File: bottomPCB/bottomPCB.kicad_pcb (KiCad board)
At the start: 2 copper layers, 184.8 x 132.4 mm, 48 parts, among them CN2 XT30UPB-F, J2 Conn_02x03_Odd_Even, J3 Conn_01x02, J4 Conn_02x03_Odd_Even, U1 ESP32-WROOM-32, U3 XT30_horizontal, U8 LM1117IMPX-3_3_NOPB, U9 LM1117IMPX-3_3_NOPB

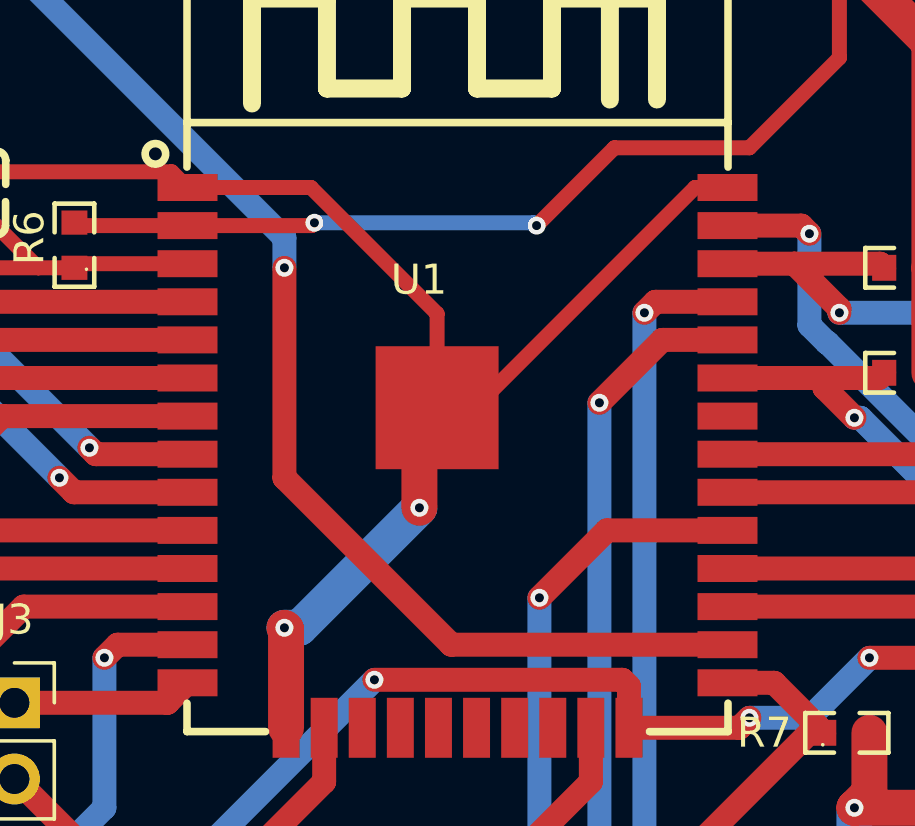
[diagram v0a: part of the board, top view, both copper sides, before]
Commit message: removed useless gnd traces
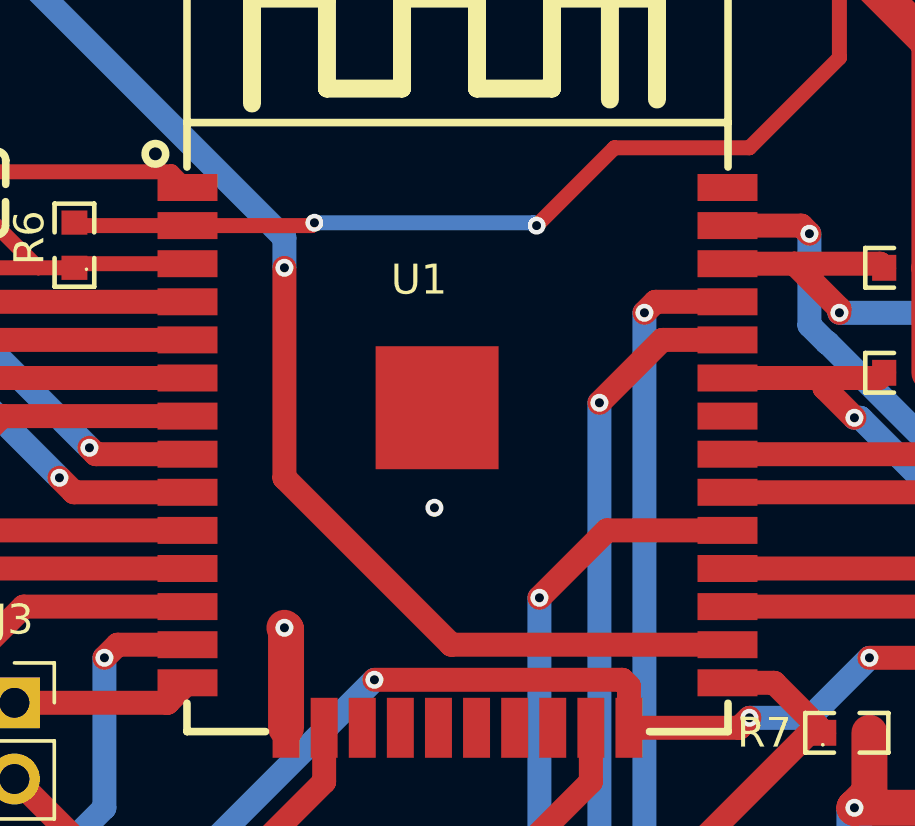
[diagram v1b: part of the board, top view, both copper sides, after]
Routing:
- net GND: track 109.5 -> 76.0 mm
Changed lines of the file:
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@@
-	)
-	(segment
-		(start 1.769622 7.823381)
-		(end 5.884042 7.823381)
-		(width 0.5)
-		(layer "F.Cu")
-		(net 1)
 	)
 	(segment
 		(start -14.539999 27.579999)
 		(end -14.5 27.54)
-		(width 1.2)
-		(layer "F.Cu")
-		(net 1)
-	)
-	(segment
-		(start 9.5 18.5)
-		(end 9.5 15.753404)
 		(width 1.2)
 		(layer "F.Cu")
@@
 	)
 	(segment
-		(start 18.689625 7.823381)
-		(end 19.769622 7.823381)
-		(width 0.5)
-		(layer "F.Cu")
-		(net 1)
-	)
-	(segment
 		(start -11.96 27.54)
 		(end -9.42 27.54)
@@
 	)
 	(segment
-		(start 5.884042 7.823381)
-		(end 10.089662 12.029001)
-		(width 0.5)
-		(layer "F.Cu")
-		(net 1)
-	)
-	(segment
 		(start 34.5 47.5)
 		(end 33.459995 46.459995)
@@
 	)
 	(segment
-		(start 11.349264 15.163742)
-		(end 18.689625 7.823381)
-		(width 0.5)
-		(layer "F.Cu")
-		(net 1)
-	)
-	(segment
 		(start 1.246217 7.299976)
 		(end 1.769622 7.823381)
@@
 		(start -5 7.299976)
 		(end 1.246217 7.299976)
-		(width 0.5)
-		(layer "F.Cu")
-		(net 1)
-	)
-	(segment
-		(start 10.089662 12.029001)
-		(end 10.089662 15.163742)
 		(width 0.5)
 		(layer "F.Cu")
@@
 	)
 	(via
-		(at 9.5 18.5)
+		(at 10 18.5)
 		(size 0.6)
 		(drill 0.3)
@@
 		(net 1)
 	)
-	(segment
-		(start 5 22.5)
-		(end 5.5 22.5)
-		(width 1.2)
-		(layer "B.Cu")
-		(net 1)
-	)
-	(segment
-		(start 5.5 22.5)
-		(end 9.5 18.5)
-		(width 1.2)
-		(layer "B.Cu")
-		(net 1)
-	)

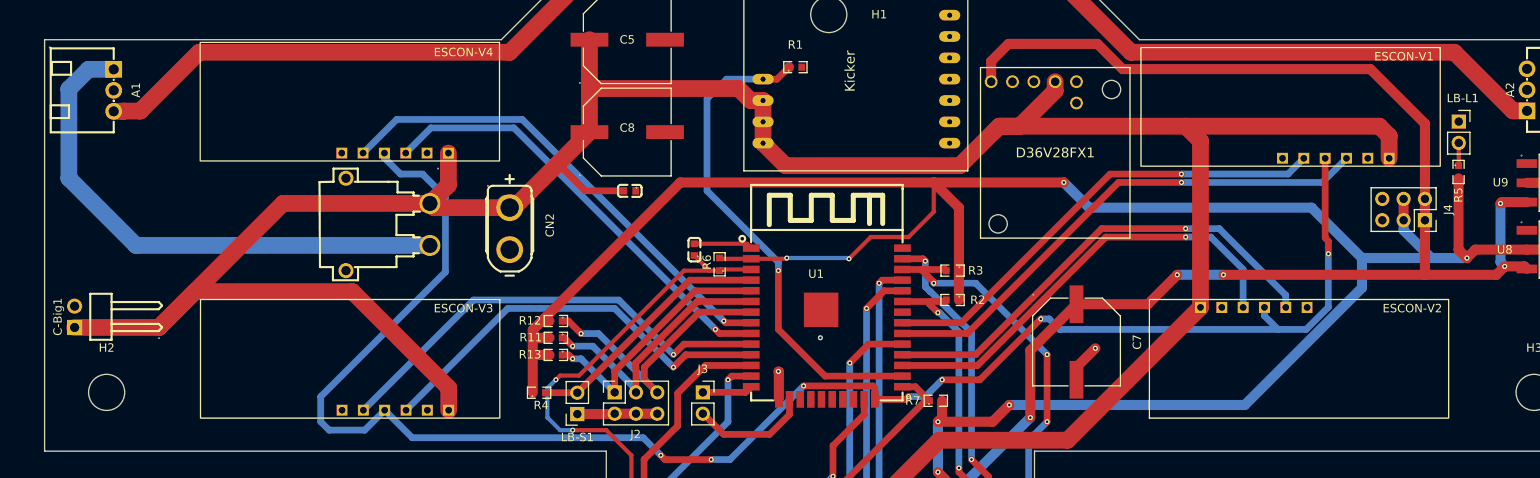
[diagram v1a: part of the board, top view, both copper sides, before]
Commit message: added silk screen (polarity, pinout)
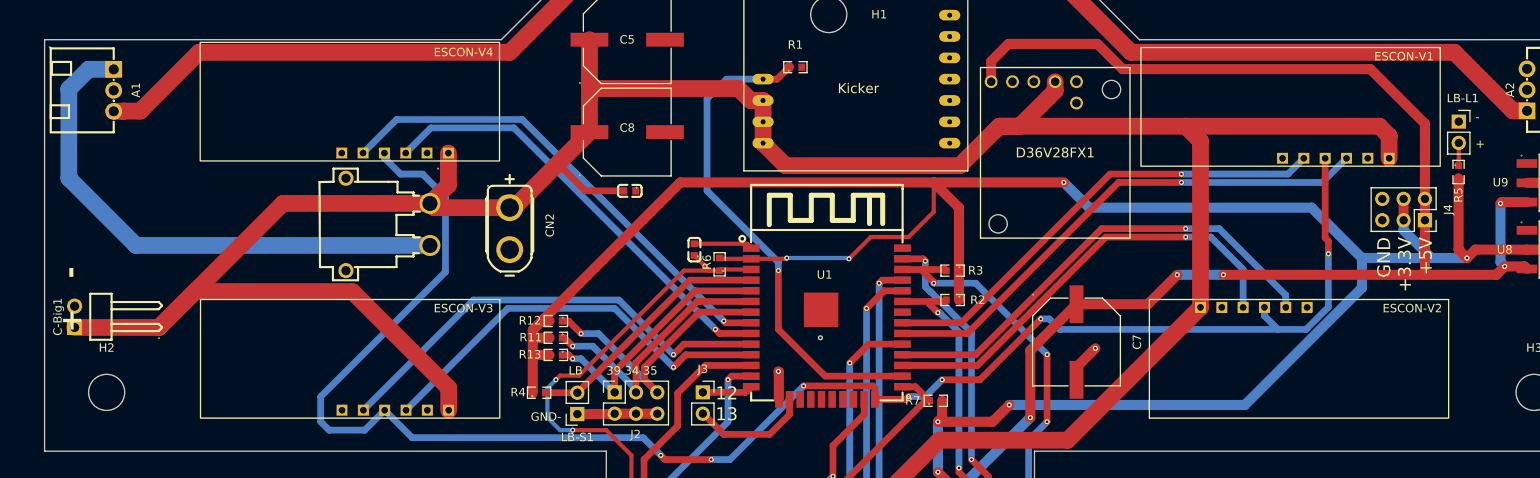
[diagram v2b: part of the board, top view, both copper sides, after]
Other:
- board text added: "- +"
- board text added: "12 13"
- board text added: "39 34 35"
- board text added: "GND +3.3V +5V"
- board text added: "GND-"
- board text added: "LB"
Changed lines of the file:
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@@
 		(tags "WIFIM-SMD_ESP32-WROOM-32-N4 footprint")
 		(property "Reference" "U1"
-			(at -1.285 -5.930001 180)
+			(at -0.269647 -5.828512 180)
 			(layer "F.SilkS")
 			(effects
@@
 		(tags "R0603 footprint")
 		(property "Reference" "R4"
-			(at 0.253366 1.5 0)
+			(at -2.5 -0.04 0)
 			(layer "F.SilkS")
 			(effects
@@
 		)
 		(fp_text user "Kicker"
-			(at 9.271 -14.224 90)
+			(at 14.5 -17 180)
 			(layer "F.SilkS")
 			(effects
@@
 		(layer "User.9")
 	)
+	(gr_text "12\n13"
+		(at -2.5 28.5 0)
+		(layer "F.SilkS")
+		(effects
+			(font
+				(size 1.54 1.54)
+				(thickness 0.1)
+			)
+			(justify left bottom)
+		)
+	)
+	(gr_text "39 34 35\n"
+		(at -15.5 23 0)
+		(layer "F.SilkS")
+		(effects
+			(font
+				(size 1 1)
+				(thickness 0.1)
+			)
+			(justify left bottom)
+		)
+	)
+	(gr_text "GND\n+3.3V\n+5V"
+		(at 83 6.5 90)
+		(layer "F.SilkS")
+		(effects
+			(font
+				(size 1.54 1.54)
+				(thickness 0.1)
+			)
+			(justify right bottom)
+		)
+	)
+	(gr_text "-\n\n+"
+		(at 88 -4 0)
+		(layer "F.SilkS")
+		(effects
+			(font
+				(size 1 1)
+				(thickness 0.1)
+			)
+			(justify left bottom)
+		)
+	)
+	(gr_text "GND-\n"
+		(at -24.5 28.5 0)
+		(layer "F.SilkS")
+		(effects
+			(font
+				(size 1 1)
+				(thickness 0.1)
+			)
+			(justify left bottom)
+		)
+	)
+	(gr_text "LB\n"
+		(at -20 23 0)
+		(layer "F.SilkS")
+		(effects
+			(font
+				(size 1 1)
+				(thickness 0.1)
+			)
+			(justify left bottom)
+		)
+	)
+	(gr_text "-   +\n"
+		(at -80.5 10 -90)
+		(layer "F.SilkS")
+		(effects
+			(font
+				(size 2.5 2.5)
+				(thickness 0.22)
+				(bold yes)
+			)
+			(justify left bottom)
+		)
+	)
 	(segment

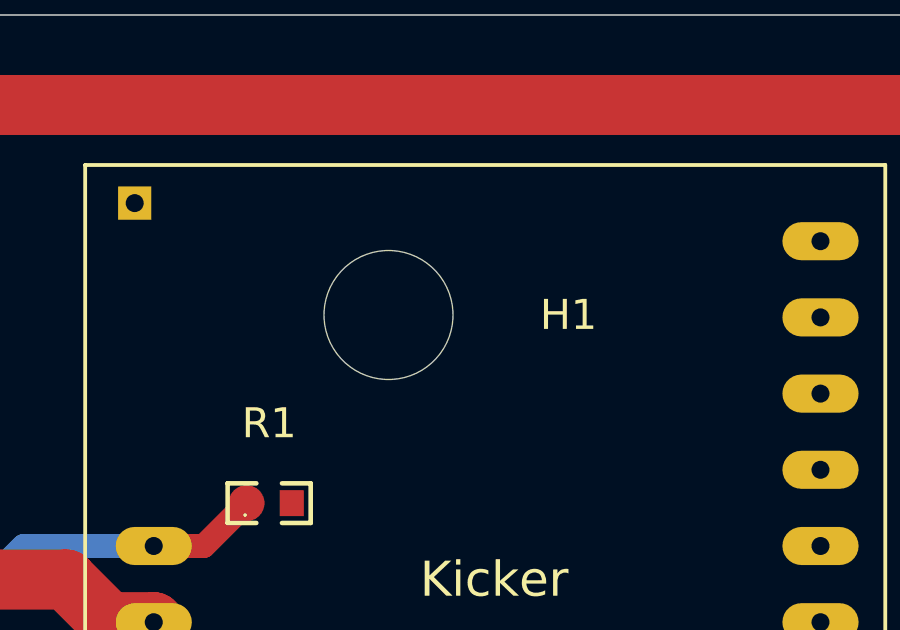
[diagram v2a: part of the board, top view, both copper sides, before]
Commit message: centered mounting hole h1
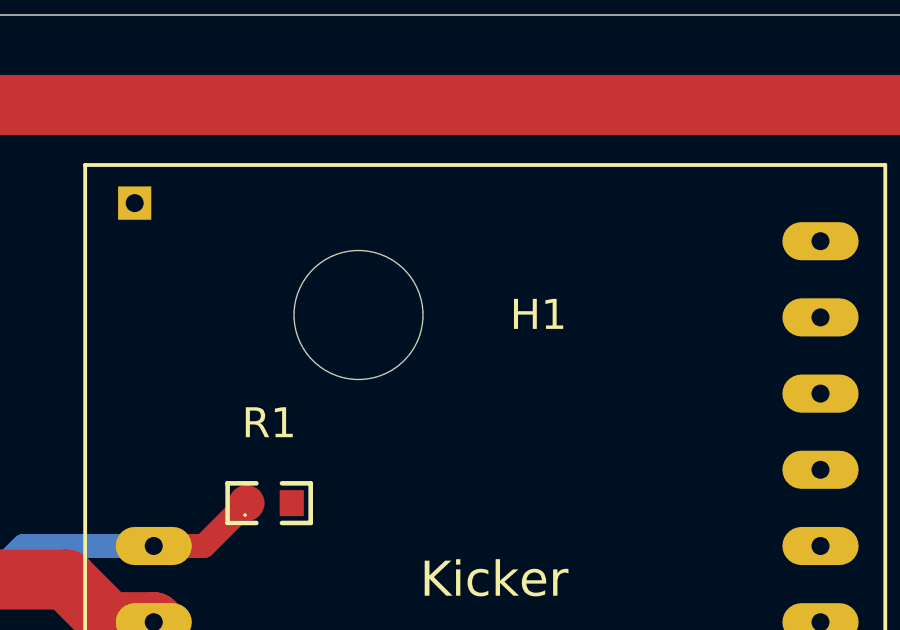
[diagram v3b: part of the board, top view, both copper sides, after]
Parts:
- moved H1 1.00 mm to (10.0, -20.0)
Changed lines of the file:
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@@
 	(footprint "BohleBots:MountingHole_4.3mm_M4"
 		(layer "F.Cu")
-		(at 11 -20)
+		(at 10 -20)
 		(descr "Mounting Hole 4.3mm, no annular, M4")
 		(tags "mounting hole 4.3mm no annular m4")

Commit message: added logo
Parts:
- added G***: LOGO, BohleBots:logo, F.Cu at (10.0, 39.0)

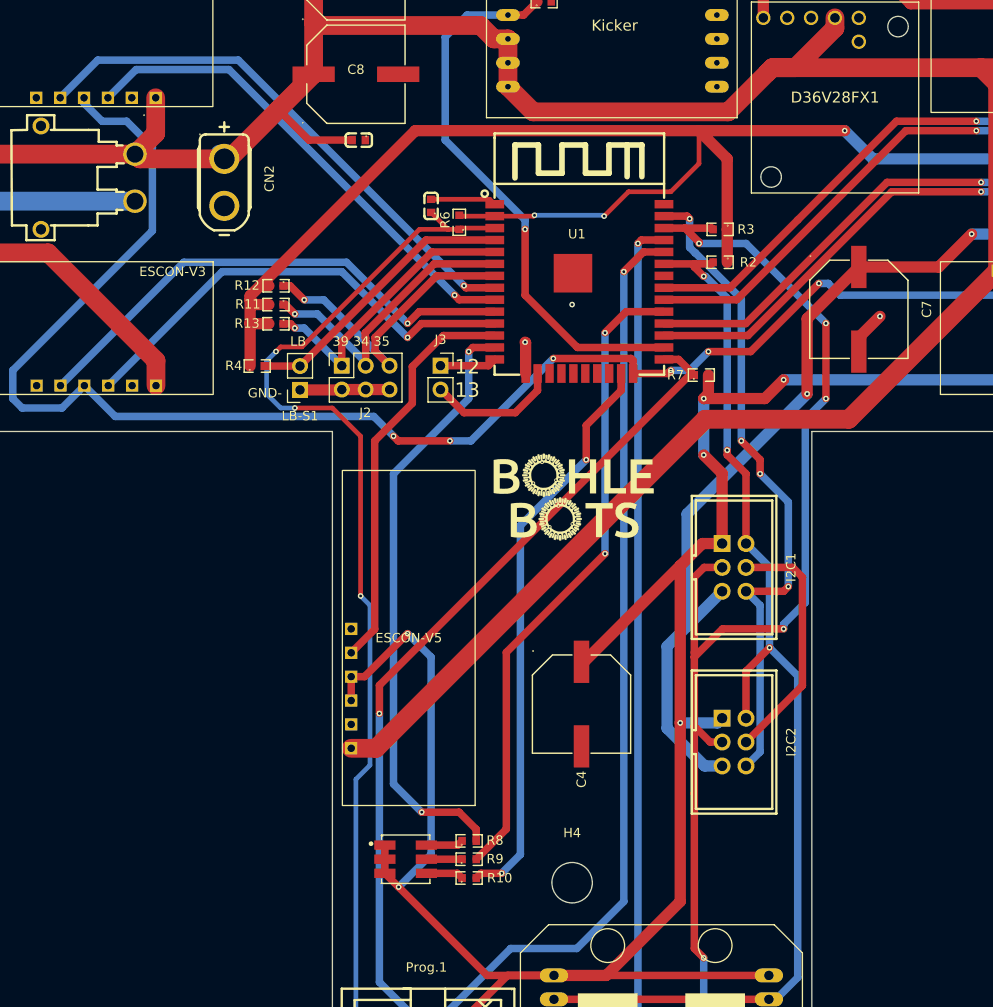
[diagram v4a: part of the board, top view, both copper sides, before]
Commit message: added GND Vias for best possible ground plane
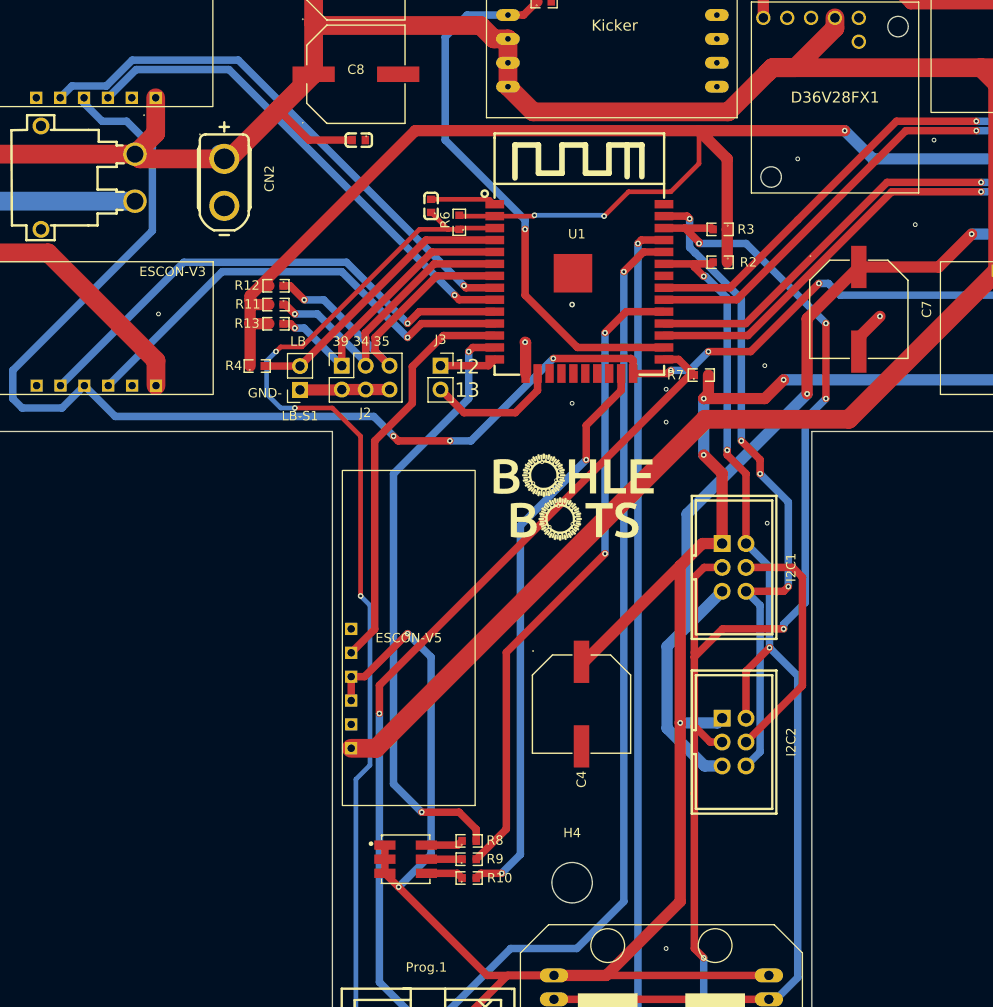
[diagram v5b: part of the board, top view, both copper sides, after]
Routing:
- net GND: vias 3 -> 13
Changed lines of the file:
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@@
 		(fp_arc
 			(start 1.390018 0.400203)
-			(mid 1.299267 0.619284)
+			(mid 1.299267 0.61928)
 			(end 1.080188 0.710033)
 			(stroke
@@
 		(fp_arc
 			(start 1.390018 0.400203)
-			(mid 1.299267 0.619284)
+			(mid 1.299267 0.61928)
 			(end 1.080188 0.710033)
 			(stroke
@@
 	)
 	(via
+		(at 30.5 25)
+		(size 0.5)
+		(drill 0.3)
+		(layers "F.Cu" "B.Cu")
+		(free yes)
+		(net 1)
+	)
+	(via
+		(at 30.75 41.75)
+		(size 0.5)
+		(drill 0.3)
+		(layers "F.Cu" "B.Cu")
+		(free yes)
+		(net 1)
+	)
+	(via
 		(at 42.75 19.75)
 		(size 0.6)
@@
 	)
 	(via
+		(at 48.5 1)
+		(size 0.5)
+		(drill 0.3)
+		(layers "F.Cu" "B.Cu")
+		(free yes)
+		(net 1)
+	)
+	(via
+		(at 20 27.5)
+		(size 0.5)
+		(drill 0.3)
+		(layers "F.Cu" "B.Cu")
+		(free yes)
+		(net 1)
+	)
+	(via
+		(at 34 3)
+		(size 0.5)
+		(drill 0.3)
+		(layers "F.Cu" "B.Cu")
+		(free yes)
+		(net 1)
+	)
+	(via
+		(at 20 87)
+		(size 0.5)
+		(drill 0.3)
+		(layers "F.Cu" "B.Cu")
+		(free yes)
+		(net 1)
+	)
+	(via
+		(at -34 19.5)
+		(size 0.5)
+		(drill 0.3)
+		(layers "F.Cu" "B.Cu")
+		(free yes)
+		(net 1)
+	)
+	(via
+		(at 20 31)
+		(size 0.5)
+		(drill 0.3)
+		(layers "F.Cu" "B.Cu")
+		(free yes)
+		(net 1)
+	)
+	(via
 		(at 10 18.5)
 		(size 0.6)
@@
 		(net 1)
 	)
+	(via
+		(at 10 29)
+		(size 0.5)
+		(drill 0.3)
+		(layers "F.Cu" "B.Cu")
+		(free yes)
+		(net 1)
+	)
+	(via
+		(at 46.5 10)
+		(size 0.5)
+		(drill 0.3)
+		(layers "F.Cu" "B.Cu")
+		(free yes)
+		(net 1)
+	)
 	(segment
 		(start 32.4 -16.5)
@@
 	)
 	(segment
-		(start -40.46 -7.5)
+		(start -39.540213 -4.754001)
+		(end -43.205999 -4.754001)
+		(width 0.8)
+		(layer "B.Cu")
+		(net 26)
+	)
+	(segment
+		(start -43.205999 -4.754001)
 		(end -44.46 -3.5)
 		(width 0.8)
@@
 	(segment
 		(start -25.5 -7.5)
-		(end -40.46 -7.5)
+		(end -36.794214 -7.5)
+		(width 0.8)
+		(layer "B.Cu")
+		(net 26)
+	)
+	(segment
+		(start -36.794214 -7.5)
+		(end -39.540213 -4.754001)
 		(width 0.8)
 		(layer "B.Cu")

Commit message: mend
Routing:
- net GND: track 76.0 -> 82.2 mm, vias 13 -> 18
- net P23: track 70.9 -> 73.4 mm
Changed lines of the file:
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@@
 	)
 	(segment
+		(start 28.5 65.040005)
+		(end 31.370002 62.170002)
+		(width 0.8)
+		(layer "F.Cu")
+		(net 1)
+	)
+	(segment
 		(start 5.054611 25.833541)
 		(end 5.054611 22.554611)
@@
 	)
 	(segment
+		(start 31.370002 62.170002)
+		(end 34.5 59.040005)
+		(width 0.8)
+		(layer "F.Cu")
+		(net 1)
+	)
+	(segment
 		(start -14.5 27.54)
 		(end -11.96 27.54)
@@
 		(net 1)
 	)
-	(segment
-		(start 28.5 65.040005)
-		(end 34.5 59.040005)
-		(width 0.8)
-		(layer "F.Cu")
-		(net 1)
-	)
 	(via
 		(at 30.5 25)
@@
 	)
 	(via
+		(at -12 73.4)
+		(size 0.6)
+		(drill 0.3)
+		(layers "F.Cu" "B.Cu")
+		(net 1)
+	)
+	(via
 		(at 10 18.5)
 		(size 0.6)
@@
 	)
 	(via
+		(at -7.2 73.4)
+		(size 0.6)
+		(drill 0.3)
+		(layers "F.Cu" "B.Cu")
+		(net 1)
+	)
+	(via
+		(at 26.6 58.6)
+		(size 0.6)
+		(drill 0.3)
+		(layers "F.Cu" "B.Cu")
+		(net 1)
+	)
+	(via
+		(at -7.2 68.8)
+		(size 0.6)
+		(drill 0.3)
+		(layers "F.Cu" "B.Cu")
+		(net 1)
+	)
+	(via
 		(at 46.5 10)
 		(size 0.5)
@@
 		(net 1)
 	)
+	(via
+		(at 31.370002 62.170002)
+		(size 0.6)
+		(drill 0.3)
+		(layers "F.Cu" "B.Cu")
+		(net 1)
+	)
+	(segment
+		(start 31.370002 62.170002)
+		(end 27.8 58.6)
+		(width 0.8)
+		(layer "B.Cu")
+		(net 1)
+	)
+	(segment
+		(start 27.8 58.6)
+		(end 26.6 58.6)
+		(width 0.8)
+		(layer "B.Cu")
+		(net 1)
+	)
 	(segment
 		(start 32.4 -16.5)
@@
 	)
 	(segment
-		(start 57.5006 5.5)
-		(end 65.4252 13.4246)
+		(start 65.4252 13.8252)
+		(end 57.1 5.5)
 		(width 0.8)
 		(layer "B.Cu")
@@
 	)
 	(segment
-		(start 65.4252 13.4246)
-		(end 65.4252 14.8786)
+		(start 53.5 5.5)
+		(end 57.1 5.5)
 		(width 0.8)
 		(layer "B.Cu")
@@
 	)
 	(segment
-		(start 53.5 5.5)
-		(end 57.5006 5.5)
+		(start 65.4252 14.8786)
+		(end 65.4252 13.8252)
 		(width 0.8)
 		(layer "B.Cu")
@@
 	)
 	(segment
-		(start 30 66.08001)
-		(end 28.5 67.58001)
+		(start 22.5 12.414214)
+		(end 22.5 9.363386)
 		(width 0.8)
 		(layer "B.Cu")
@@
 	)
 	(segment
-		(start 22.5 12.414214)
-		(end 22.5 9.363386)
+		(start 33 48.5)
+		(end 33 39.5)
 		(width 0.8)
 		(layer "B.Cu")
@@
 	(segment
 		(start 30 50.5)
-		(end 30 66.08001)
+		(end 29.999999 54.585787)
 		(width 0.8)
 		(layer "B.Cu")
@@
 	)
 	(segment
-		(start 28.5 49)
-		(end 30 50.5)
+		(start 28 33)
+		(end 28 17.88873)
 		(width 0.8)
 		(layer "B.Cu")
@@
 	)
 	(segment
-		(start 33 48.5)
-		(end 33 39.5)
+		(start 29.999999 54.585787)
+		(end 29.999999 55.414213)
 		(width 0.8)
 		(layer "B.Cu")
@@
 	)
 	(segment
-		(start 28 33)
-		(end 28 17.88873)
+		(start 33 58.414214)
+		(end 33 63.08001)
+		(width 0.8)
+		(layer "B.Cu")
+		(net 42)
+	)
+	(segment
+		(start 33 63.08001)
+		(end 28.5 67.58001)
+		(width 0.8)
+		(layer "B.Cu")
+		(net 42)
+	)
+	(segment
+		(start 28.5 49)
+		(end 30 50.5)
 		(width 0.8)
 		(layer "B.Cu")
@@
 		(width 0.8)
 		(layer "B.Cu")
+		(net 42)
+	)
+	(segment
+		(start 29.999999 55.414213)
+		(end 33 58.414214)
+		(width 0.8)
+		(layer "B.Cu")

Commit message: V2.0
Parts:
- added G***: LOGO, sarcat:sarcatLabelSmall, F.Cu at (89.6, 14.8)
- added G***: LOGO, sarcat:sarcatLogoSmall, F.Cu at (-70.8, 3.20)
- added G***: LOGO, sarcat:sarcatLabel, B.Cu at (10.0, 55.8)
- added G***: LOGO, sarcat:sarcatLogo, B.Cu at (10.0, 10.0)
